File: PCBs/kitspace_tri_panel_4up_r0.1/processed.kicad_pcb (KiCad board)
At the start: 4 copper layers, 105.3 x 45.2 mm, 660 parts, among them J1 input, J2 output, Q1 LP0404N3T5G, Q10 LP0404N3T5G, Q11 LP0404N3T5G, Q12 LP0404N3T5G, Q13 LP0404N3T5G, Q14 LP0404N3T5G, Q15 LP0404N3T5G, Q2 LP0404N3T5G, Q3 LP0404N3T5G, Q4 LP0404N3T5G, Q5 LP0404N3T5G, Q6 LP0404N3T5G, Q7 LP0404N3T5G, Q8 LP0404N3T5G, Q9 LP0404N3T5G, U1 TLC59025, U2 TLC59025, U3 TLC59025, U4 74HC595, U5 74HC595

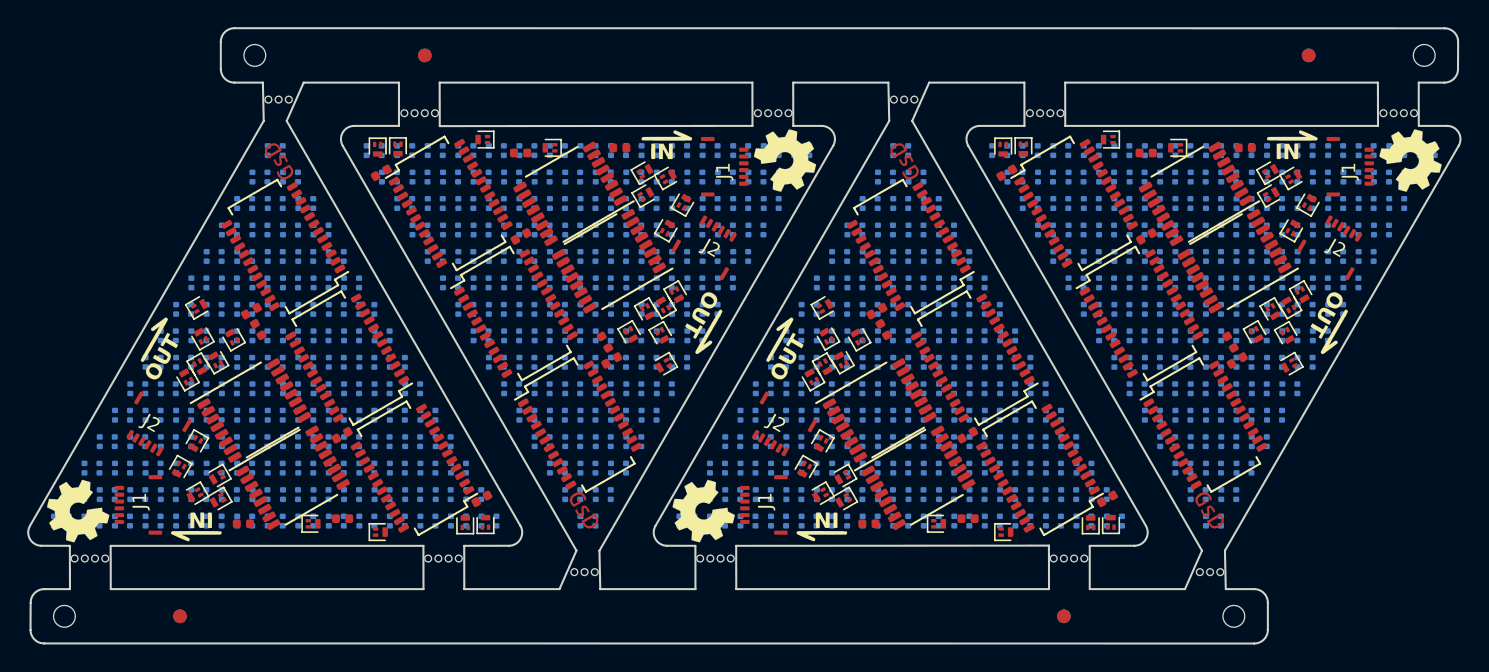
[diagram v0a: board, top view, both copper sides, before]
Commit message: recheck all circuits and clean up fill zone by rerouting the nets using freerouting and manually
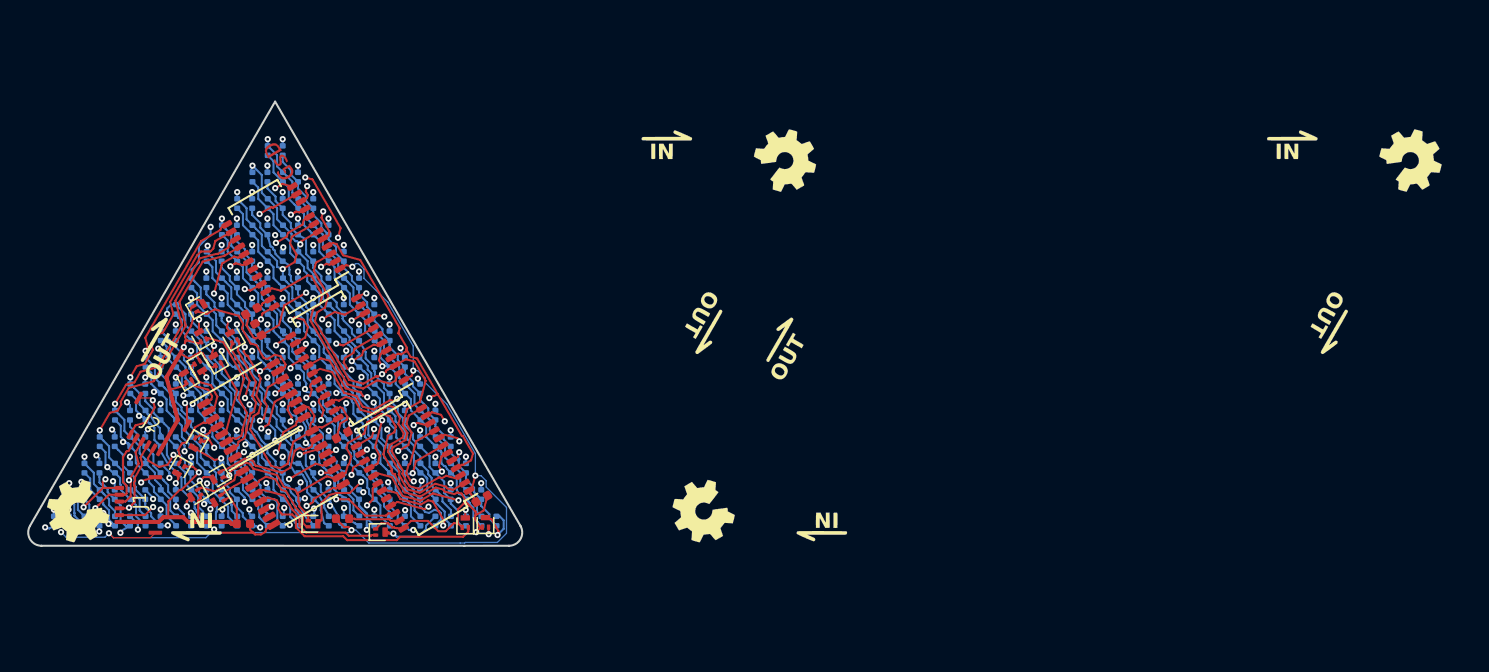
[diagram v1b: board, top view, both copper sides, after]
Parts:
- removed ? (x4): , MountingHole:MountingHole_2.1mm
- removed the C1 at (121.8, 91.6)
- removed the C1 at (167.8, 91.6)
- removed the C1 at (175.2, 115.6)
- removed the C2 at (138.2, 104.1)
- removed the C2 at (184.2, 104.1)
- removed the C2 at (158.8, 103.2)
- removed the C3 at (139.3, 89.8)
- removed the C3 at (185.3, 89.8)
- removed the C3 at (157.7, 117.4)
- removed the D1 at (137.0, 117.2)
- removed the D1 at (183.0, 117.2)
- removed the D1 at (160.0, 90.0)
- removed the D10 at (147.1, 99.7)
- removed the D10 at (193.1, 99.7)
- removed the D10 at (149.9, 107.5)
- removed the D100 at (133.6, 99.7)
- removed the D100 at (179.6, 99.7)
- removed the D100 at (163.4, 107.5)
- removed the D101 at (134.8, 97.8)
- removed the D101 at (180.8, 97.8)
- removed the D101 at (162.2, 109.5)
- removed the D102 at (135.9, 95.8)
- removed the D102 at (181.9, 95.8)
- removed the D102 at (161.1, 111.4)
- removed the D103 at (137.0, 93.9)
- removed the D103 at (183.0, 93.9)
- removed the D103 at (160.0, 113.4)
- removed the D104 at (138.1, 91.9)
- removed the D104 at (184.1, 91.9)
- removed the D104 at (158.9, 115.3)
- removed the D105 at (139.2, 90.0)
- removed the D105 at (185.2, 90.0)
- removed the D105 at (157.8, 117.2)
- removed the D11 at (148.2, 97.8)
- removed the D11 at (194.2, 97.8)
- removed the D11 at (148.8, 109.5)
- removed the D113 at (129.1, 103.6)
- removed the D113 at (175.1, 103.6)
- removed the D113 at (167.9, 103.6)
- removed the D114 at (130.3, 101.7)
- removed the D114 at (176.3, 101.7)
- removed the D114 at (166.7, 105.6)
- removed the D115 at (131.4, 99.7)
- removed the D115 at (177.4, 99.7)
- removed the D115 at (165.6, 107.5)
- removed the D116 at (132.5, 97.8)
- removed the D116 at (178.5, 97.8)
- removed the D116 at (164.5, 109.5)
- removed the D117 at (133.6, 95.8)
- removed the D117 at (179.6, 95.8)
- removed the D117 at (163.4, 111.4)
- removed the D118 at (134.8, 93.9)
- removed the D118 at (180.8, 93.9)
- removed the D118 at (162.2, 113.4)
- removed the D119 at (135.9, 91.9)
- removed the D119 at (181.9, 91.9)
- removed the D119 at (161.1, 115.3)
- removed the D12 at (149.4, 95.8)
- removed the D12 at (195.4, 95.8)
- removed the D12 at (147.6, 111.4)
- removed the D120 at (137.0, 90.0)
- removed the D120 at (183.0, 90.0)
- removed the D120 at (160.0, 117.2)
- removed the D129 at (128.0, 101.7)
- removed the D129 at (174.0, 101.7)
- removed the D129 at (169.0, 105.6)
- removed the D13 at (150.5, 93.9)
- removed the D13 at (196.5, 93.9)
- removed the D13 at (146.5, 113.4)
- removed the D130 at (129.1, 99.7)
- removed the D130 at (175.1, 99.7)
- removed the D130 at (167.9, 107.5)
- removed the D131 at (130.3, 97.8)
- removed the D131 at (176.3, 97.8)
- removed the D131 at (166.7, 109.5)
- removed the D132 at (131.4, 95.8)
- removed the D132 at (177.4, 95.8)
- removed the D132 at (165.6, 111.4)
- removed the D133 at (132.5, 93.9)
- removed the D133 at (178.5, 93.9)
- removed the D133 at (164.5, 113.4)
- removed the D134 at (133.6, 91.9)
- removed the D134 at (179.6, 91.9)
- removed the D134 at (163.4, 115.3)
- removed the D135 at (134.8, 90.0)
- removed the D135 at (180.8, 90.0)
- removed the D135 at (162.2, 117.2)
- removed the D14 at (151.6, 91.9)
- removed the D14 at (197.6, 91.9)
- removed the D14 at (145.4, 115.3)
- removed the D145 at (126.9, 99.7)
- removed the D145 at (172.9, 99.7)
- removed the D145 at (170.1, 107.5)
- removed the D146 at (128.0, 97.8)
- removed the D146 at (174.0, 97.8)
- removed the D146 at (169.0, 109.5)
- removed the D147 at (129.1, 95.8)
- removed the D147 at (175.1, 95.8)
- removed the D147 at (167.9, 111.4)
- removed the D148 at (130.3, 93.9)
- removed the D148 at (176.3, 93.9)
- removed the D148 at (166.7, 113.4)
- removed the D149 at (131.4, 91.9)
- removed the D149 at (177.4, 91.9)
- removed the D149 at (165.6, 115.3)
- removed the D15 at (152.7, 90.0)
- removed the D15 at (198.7, 90.0)
- removed the D15 at (144.3, 117.2)
- removed the D150 at (132.5, 90.0)
- removed the D150 at (178.5, 90.0)
- removed the D150 at (164.5, 117.2)
- removed the D161 at (125.8, 97.8)
- removed the D161 at (171.8, 97.8)
- removed the D161 at (171.2, 109.5)
- removed the D162 at (126.9, 95.8)
- removed the D162 at (172.9, 95.8)
- removed the D162 at (170.1, 111.4)
- removed the D163 at (128.0, 93.9)
- removed the D163 at (174.0, 93.9)
- removed the D163 at (169.0, 113.4)
- removed the D164 at (129.1, 91.9)
- removed the D164 at (175.1, 91.9)
- removed the D164 at (167.9, 115.3)
- removed the D165 at (130.3, 90.0)
- removed the D165 at (176.3, 90.0)
- removed the D165 at (166.7, 117.2)
- removed the D17 at (135.9, 115.3)
- removed the D17 at (181.9, 115.3)
- removed the D17 at (161.1, 91.9)
- removed the D177 at (124.6, 95.8)
- removed the D177 at (170.6, 95.8)
- removed the D177 at (172.4, 111.4)
- removed the D178 at (125.8, 93.9)
- removed the D178 at (171.8, 93.9)
- removed the D178 at (171.2, 113.4)
- removed the D179 at (126.9, 91.9)
- removed the D179 at (172.9, 91.9)
- removed the D179 at (170.1, 115.3)
- removed the D18 at (137.0, 113.4)
- removed the D18 at (183.0, 113.4)
- removed the D18 at (160.0, 93.9)
- removed the D180 at (128.0, 90.0)
- removed the D180 at (174.0, 90.0)
- removed the D180 at (169.0, 117.2)
- removed the D19 at (138.1, 111.4)
- removed the D19 at (184.1, 111.4)
- removed the D19 at (158.9, 95.8)
- removed the D193 at (123.5, 93.9)
- removed the D193 at (169.5, 93.9)
- removed the D193 at (173.5, 113.4)
- removed the D194 at (124.6, 91.9)
- removed the D194 at (170.6, 91.9)
- removed the D194 at (172.4, 115.3)
- removed the D195 at (125.8, 90.0)
- removed the D195 at (171.8, 90.0)
- removed the D195 at (171.2, 117.2)
- removed the D2 at (138.1, 115.3)
- removed the D2 at (184.1, 115.3)
- removed the D2 at (158.9, 91.9)
- removed the D20 at (139.2, 109.5)
- removed the D20 at (185.2, 109.5)
- removed the D20 at (157.8, 97.8)
- removed the D209 at (122.4, 91.9)
- removed the D209 at (168.4, 91.9)
- removed the D209 at (174.6, 115.3)
- removed the D21 at (140.4, 107.5)
- removed the D21 at (186.4, 107.5)
- removed the D21 at (156.6, 99.7)
- removed the D210 at (123.5, 90.0)
- removed the D210 at (169.5, 90.0)
- removed the D210 at (173.5, 117.2)
- removed the D22 at (141.5, 105.6)
- removed the D22 at (187.5, 105.6)
- removed the D22 at (155.5, 101.7)
- removed the D225 at (121.3, 90.0)
- removed the D225 at (167.3, 90.0)
- removed the D225 at (175.7, 117.2)
- removed the D23 at (142.6, 103.6)
- removed the D23 at (188.6, 103.6)
- removed the D23 at (154.4, 103.6)
- removed the D24 at (143.7, 101.7)
- removed the D24 at (189.7, 101.7)
- removed the D24 at (153.3, 105.6)
- removed the D25 at (144.9, 99.7)
- removed the D25 at (190.9, 99.7)
- removed the D25 at (152.1, 107.5)
- removed the D26 at (146.0, 97.8)
- removed the D26 at (192.0, 97.8)
- removed the D26 at (151.0, 109.5)
- removed the D27 at (147.1, 95.8)
- removed the D27 at (193.1, 95.8)
- removed the D27 at (149.9, 111.4)
- removed the D28 at (148.2, 93.9)
- removed the D28 at (194.2, 93.9)
- removed the D28 at (148.8, 113.4)
- removed the D29 at (149.4, 91.9)
- removed the D29 at (195.4, 91.9)
- removed the D29 at (147.6, 115.3)
- removed the D3 at (139.2, 113.4)
- removed the D3 at (185.2, 113.4)
- removed the D3 at (157.8, 93.9)
- removed the D30 at (150.5, 90.0)
- removed the D30 at (196.5, 90.0)
- removed the D30 at (146.5, 117.2)
- removed the D33 at (134.8, 113.4)
- removed the D33 at (180.8, 113.4)
- removed the D33 at (162.2, 93.9)
- removed the D34 at (135.9, 111.4)
- removed the D34 at (181.9, 111.4)
- removed the D34 at (161.1, 95.8)
- removed the D35 at (137.0, 109.5)
- removed the D35 at (183.0, 109.5)
- removed the D35 at (160.0, 97.8)
- removed the D36 at (138.1, 107.5)
- removed the D36 at (184.1, 107.5)
- removed the D36 at (158.9, 99.7)
- removed the D37 at (139.2, 105.6)
- removed the D37 at (185.2, 105.6)
- removed the D37 at (157.8, 101.7)
- removed the D38 at (140.4, 103.6)
- removed the D38 at (186.4, 103.6)
- removed the D38 at (156.6, 103.6)
- removed the D39 at (141.5, 101.7)
- removed the D39 at (187.5, 101.7)
- removed the D39 at (155.5, 105.6)
- removed the D4 at (140.4, 111.4)
- removed the D4 at (186.4, 111.4)
- removed the D4 at (156.6, 95.8)
- removed the D40 at (142.6, 99.7)
- removed the D40 at (188.6, 99.7)
- removed the D40 at (154.4, 107.5)
- removed the D41 at (143.7, 97.8)
- removed the D41 at (189.7, 97.8)
- removed the D41 at (153.3, 109.5)
- removed the D42 at (144.9, 95.8)
- removed the D42 at (190.9, 95.8)
- removed the D42 at (152.1, 111.4)
- removed the D43 at (146.0, 93.9)
- removed the D43 at (192.0, 93.9)
- removed the D43 at (151.0, 113.4)
- removed the D44 at (147.1, 91.9)
- removed the D44 at (193.1, 91.9)
- removed the D44 at (149.9, 115.3)
- removed the D45 at (148.2, 90.0)
- removed the D45 at (194.2, 90.0)
- removed the D45 at (148.8, 117.2)
- removed the D49 at (133.6, 111.4)
- removed the D49 at (179.6, 111.4)
- removed the D49 at (163.4, 95.8)
- removed the D5 at (141.5, 109.5)
- removed the D5 at (187.5, 109.5)
- removed the D5 at (155.5, 97.8)
- removed the D50 at (134.8, 109.5)
- removed the D50 at (180.8, 109.5)
- removed the D50 at (162.2, 97.8)
- removed the D51 at (135.9, 107.5)
- removed the D51 at (181.9, 107.5)
- removed the D51 at (161.1, 99.7)
- removed the D52 at (137.0, 105.6)
- removed the D52 at (183.0, 105.6)
- removed the D52 at (160.0, 101.7)
- removed the D53 at (138.1, 103.6)
- removed the D53 at (184.1, 103.6)
- removed the D53 at (158.9, 103.6)
- removed the D54 at (139.2, 101.7)
- removed the D54 at (185.2, 101.7)
- removed the D54 at (157.8, 105.6)
- removed the D55 at (140.4, 99.7)
- removed the D55 at (186.4, 99.7)
- removed the D55 at (156.6, 107.5)
- removed the D56 at (141.5, 97.8)
- removed the D56 at (187.5, 97.8)
- removed the D56 at (155.5, 109.5)
- removed the D57 at (142.6, 95.8)
- removed the D57 at (188.6, 95.8)
- removed the D57 at (154.4, 111.4)
- removed the D58 at (143.7, 93.9)
- removed the D58 at (189.7, 93.9)
- removed the D58 at (153.3, 113.4)
- removed the D59 at (144.9, 91.9)
- removed the D59 at (190.9, 91.9)
- removed the D59 at (152.1, 115.3)
- removed the D6 at (142.6, 107.5)
- removed the D6 at (188.6, 107.5)
- removed the D6 at (154.4, 99.7)
- removed the D60 at (146.0, 90.0)
- removed the D60 at (192.0, 90.0)
- removed the D60 at (151.0, 117.2)
- removed the D65 at (132.5, 109.5)
- removed the D65 at (178.5, 109.5)
- removed the D65 at (164.5, 97.8)
- removed the D66 at (133.6, 107.5)
- removed the D66 at (179.6, 107.5)
- removed the D66 at (163.4, 99.7)
- removed the D67 at (134.8, 105.6)
- removed the D67 at (180.8, 105.6)
- removed the D67 at (162.2, 101.7)
- removed the D68 at (135.9, 103.6)
- removed the D68 at (181.9, 103.6)
- removed the D68 at (161.1, 103.6)
- removed the D69 at (137.0, 101.7)
- removed the D69 at (183.0, 101.7)
- removed the D69 at (160.0, 105.6)
- removed the D7 at (143.7, 105.6)
- removed the D7 at (189.7, 105.6)
- removed the D7 at (153.3, 101.7)
- removed the D70 at (138.1, 99.7)
- removed the D70 at (184.1, 99.7)
- removed the D70 at (158.9, 107.5)
- removed the D71 at (139.2, 97.8)
- removed the D71 at (185.2, 97.8)
- removed the D71 at (157.8, 109.5)
- removed the D72 at (140.4, 95.8)
- removed the D72 at (186.4, 95.8)
- removed the D72 at (156.6, 111.4)
- removed the D73 at (141.5, 93.9)
- removed the D73 at (187.5, 93.9)
- removed the D73 at (155.5, 113.4)
- removed the D74 at (142.6, 91.9)
- removed the D74 at (188.6, 91.9)
- removed the D74 at (154.4, 115.3)
- removed the D75 at (143.7, 90.0)
- removed the D75 at (189.7, 90.0)
- removed the D75 at (153.3, 117.2)
- removed the D8 at (144.9, 103.6)
- removed the D8 at (190.9, 103.6)
- removed the D8 at (152.1, 103.6)
- removed the D81 at (131.4, 107.5)
- removed the D81 at (177.4, 107.5)
- removed the D81 at (165.6, 99.7)
- removed the D82 at (132.5, 105.6)
- removed the D82 at (178.5, 105.6)
- removed the D82 at (164.5, 101.7)
- removed the D83 at (133.6, 103.6)
- removed the D83 at (179.6, 103.6)
- removed the D83 at (163.4, 103.6)
- removed the D84 at (134.8, 101.7)
- removed the D84 at (180.8, 101.7)
- removed the D84 at (162.2, 105.6)
- removed the D85 at (135.9, 99.7)
- removed the D85 at (181.9, 99.7)
- removed the D85 at (161.1, 107.5)
- removed the D86 at (137.0, 97.8)
- removed the D86 at (183.0, 97.8)
- removed the D86 at (160.0, 109.5)
- removed the D87 at (138.1, 95.8)
- removed the D87 at (184.1, 95.8)
- removed the D87 at (158.9, 111.4)
- removed the D88 at (139.2, 93.9)
- removed the D88 at (185.2, 93.9)
- removed the D88 at (157.8, 113.4)
- removed the D89 at (140.4, 91.9)
- removed the D89 at (186.4, 91.9)
- removed the D89 at (156.6, 115.3)
- removed the D9 at (146.0, 101.7)
- removed the D9 at (192.0, 101.7)
- removed the D9 at (151.0, 105.6)
- removed the D90 at (141.5, 90.0)
- removed the D90 at (187.5, 90.0)
- removed the D90 at (155.5, 117.2)
- removed the D97 at (130.3, 105.6)
- removed the D97 at (176.3, 105.6)
- removed the D97 at (166.7, 101.7)
- removed the D98 at (131.4, 103.6)
- removed the D98 at (177.4, 103.6)
- removed the D98 at (165.6, 103.6)
- removed the D99 at (132.5, 101.7)
- removed the D99 at (178.5, 101.7)
- removed the D99 at (164.5, 105.6)
- removed the G*** at (136.6, 116.5)
- removed the G*** at (182.6, 116.5)
- removed the G*** at (160.4, 90.7)
- removed the J1 at (148.5, 91.2)
- removed the J1 at (194.5, 91.2)
- removed the J1 at (148.5, 116.1)
- removed the J2 at (146.6, 95.7)
- removed the J2 at (192.6, 95.7)
- removed the J2 at (150.4, 111.5)
- removed the Q1 at (142.6, 105.8)
- removed the Q1 at (188.6, 105.8)
- removed the Q1 at (154.4, 101.5)
- removed the Q10 at (142.9, 91.9)
- removed the Q10 at (188.9, 91.9)
- removed the Q10 at (154.1, 115.3)
- removed the Q11 at (141.2, 91.5)
- removed the Q11 at (187.2, 91.5)
- removed the Q11 at (155.8, 115.7)
- removed the Q12 at (134.2, 89.8)
- removed the Q12 at (180.2, 89.8)
- removed the Q12 at (162.8, 117.4)
- removed the Q13 at (129.3, 89.2)
- removed the Q13 at (175.3, 89.2)
- removed the Q13 at (167.7, 118.1)
- removed the Q14 at (123.0, 89.9)
- removed the Q14 at (169.0, 89.9)
- removed the Q14 at (174.0, 117.4)
- removed the Q15 at (121.5, 89.9)
- removed the Q15 at (167.5, 89.9)
- removed the Q15 at (175.5, 117.3)
- removed the Q2 at (143.5, 100.6)
- removed the Q2 at (189.5, 100.6)
- removed the Q2 at (153.5, 106.7)
- removed the Q3 at (142.6, 101.4)
- removed the Q3 at (188.6, 101.4)
- removed the Q3 at (154.4, 105.9)
- removed the Q4 at (144.1, 93.8)
- removed the Q4 at (190.1, 93.8)
- removed the Q4 at (152.9, 113.4)
- removed the Q5 at (142.8, 95.7)
- removed the Q5 at (188.8, 95.7)
- removed the Q5 at (154.2, 111.5)
- removed the Q6 at (141.4, 101.8)
- removed the Q6 at (187.4, 101.8)
- removed the Q6 at (155.6, 105.4)
- removed the Q7 at (142.4, 103.6)
- removed the Q7 at (188.4, 103.6)
- removed the Q7 at (154.6, 103.7)
- removed the Q8 at (140.1, 103.5)
- removed the Q8 at (186.1, 103.5)
- removed the Q8 at (156.9, 103.7)
- removed the Q9 at (141.3, 93.2)
- removed the Q9 at (187.3, 93.2)
- removed the Q9 at (155.7, 114.0)
- removed the R1 at (138.8, 105.4)
- removed the R1 at (184.8, 105.4)
- removed the R1 at (158.2, 101.8)
- removed the R2 at (132.1, 96.3)
- removed the R2 at (178.1, 96.3)
- removed the R2 at (164.9, 110.9)
- removed the R3 at (132.0, 90.2)
- removed the R3 at (178.0, 90.2)
- removed the R3 at (165.0, 117.1)
- removed the REF** at (107.0, 124.2) (x2)
- removed the REF** at (100.8, 120.0)
- removed the REF** at (99.2, 120.0)
- removed the REF** at (125.2, 120.0)
- removed the REF** at (100.0, 120.0)
- removed the REF** at (136.8, 121.0)
- removed the REF** at (126.8, 120.0)
- removed the REF** at (127.5, 120.0)
- removed the REF** at (136.0, 121.0)
- removed the REF** at (183.5, 121.0)
- removed the REF** at (182.8, 121.0)
- removed the REF** at (172.0, 124.2) (x2)
- removed the REF** at (182.0, 121.0)
- removed the REF** at (173.5, 120.0)
- removed the REF** at (172.8, 120.0)
- removed the REF** at (172.0, 120.0)
- removed the REF** at (171.2, 120.0)
- removed the REF** at (147.5, 120.0)
- removed the REF** at (146.8, 120.0)
- removed the REF** at (146.0, 120.0)
- removed the REF** at (145.2, 120.0)
- removed the REF** at (159.5, 86.2)
- removed the REF** at (160.2, 86.2)
- removed the REF** at (161.0, 86.2)
- removed the REF** at (169.5, 87.2)
- removed the REF** at (170.2, 87.2)
- removed the REF** at (171.0, 87.2)
- removed the REF** at (171.8, 87.2)
- removed the REF** at (195.5, 87.2)
- removed the REF** at (196.2, 87.2)
- removed the REF** at (197.0, 87.2)
- removed the REF** at (197.8, 87.2)
- removed the REF** at (151.8, 87.2)
- removed the REF** at (151.0, 87.2)
- removed the REF** at (150.2, 87.2)
- removed the REF** at (149.5, 87.2)
- removed the REF** at (125.8, 87.2)
- removed the REF** at (125.0, 87.2)
- removed the REF** at (124.2, 87.2)
- removed the REF** at (190.0, 83.0) (x2)
- removed the REF** at (123.5, 87.2)
- removed the REF** at (115.0, 86.2)
- removed the REF** at (114.2, 86.2)
- removed the REF** at (113.5, 86.2)
- removed the REF** at (125.0, 83.0) (x2)
- removed the REF** at (126.0, 120.0)
- removed the REF** at (101.5, 120.0)
- removed the REF** at (137.5, 121.0)
- removed the U1 at (136.4, 110.2)
- removed the U1 at (182.4, 110.2)
- removed the U1 at (160.6, 97.1)
- removed the U2 at (131.7, 102.0)
- removed the U2 at (177.7, 102.0)
- removed the U2 at (165.3, 105.3)
- removed the U3 at (126.9, 93.9)
- removed the U3 at (172.9, 93.9)
- removed the U3 at (170.1, 113.4)
- removed the U4 at (138.6, 98.1)
- removed the U4 at (184.6, 98.1)
- removed the U4 at (158.4, 109.1)
- removed the U5 at (135.7, 93.2)
- removed the U5 at (181.7, 93.2)
- removed the U5 at (161.3, 114.1)
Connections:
- C1 pad 1: (no net) -> vcc
- C1 pad 2: (no net) -> gnd
- C2 pad 1: (no net) -> vcc
- C2 pad 2: (no net) -> gnd
- C3 pad 1: (no net) -> vcc
- C3 pad 2: (no net) -> gnd
- D1 pad 1: (no net) -> row_0
- D1 pad 2: (no net) -> colr_0
- D1 pad 3: (no net) -> colg_0
- D1 pad 4: (no net) -> colb_0
- D10 pad 1: (no net) -> row_0
- D10 pad 2: (no net) -> colr_9
- D10 pad 3: (no net) -> colg_9
- D10 pad 4: (no net) -> colb_9
- D100 pad 1: (no net) -> row_6
- D100 pad 2: (no net) -> colr_3
- D100 pad 3: (no net) -> colg_3
- D100 pad 4: (no net) -> colb_3
- D101 pad 1: (no net) -> row_6
- D101 pad 2: (no net) -> colr_4
- D101 pad 3: (no net) -> colg_4
- D101 pad 4: (no net) -> colb_4
- D102 pad 1: (no net) -> row_6
- D102 pad 2: (no net) -> colr_5
- D102 pad 3: (no net) -> colg_5
- D102 pad 4: (no net) -> colb_5
- D103 pad 1: (no net) -> row_6
- D103 pad 2: (no net) -> colr_6
- D103 pad 3: (no net) -> colg_6
- D103 pad 4: (no net) -> colb_6
- D104 pad 1: (no net) -> row_6
- D104 pad 2: (no net) -> colr_7
- D104 pad 3: (no net) -> colg_7
- D104 pad 4: (no net) -> colb_7
- D105 pad 1: (no net) -> row_6
- D105 pad 2: (no net) -> colr_8
- D105 pad 3: (no net) -> colg_8
- D105 pad 4: (no net) -> colb_8
- D11 pad 1: (no net) -> row_0
- D11 pad 2: (no net) -> colr_10
- D11 pad 3: (no net) -> colg_10
- D11 pad 4: (no net) -> colb_10
- D113 pad 1: (no net) -> row_7
- D113 pad 2: (no net) -> colr_0
- D113 pad 3: (no net) -> colg_0
- D113 pad 4: (no net) -> colb_0
- D114 pad 1: (no net) -> row_7
- D114 pad 2: (no net) -> colr_1
- D114 pad 3: (no net) -> colg_1
- D114 pad 4: (no net) -> colb_1
- D115 pad 1: (no net) -> row_7
- D115 pad 2: (no net) -> colr_2
- D115 pad 3: (no net) -> colg_2
- D115 pad 4: (no net) -> colb_2
- D116 pad 1: (no net) -> row_7
- D116 pad 2: (no net) -> colr_3
- D116 pad 3: (no net) -> colg_3
- D116 pad 4: (no net) -> colb_3
- D117 pad 1: (no net) -> row_7
- D117 pad 2: (no net) -> colr_4
- D117 pad 3: (no net) -> colg_4
- D117 pad 4: (no net) -> colb_4
- D118 pad 1: (no net) -> row_7
- D118 pad 2: (no net) -> colr_5
- D118 pad 3: (no net) -> colg_5
- D118 pad 4: (no net) -> colb_5
- D119 pad 1: (no net) -> row_7
- D119 pad 2: (no net) -> colr_6
- D119 pad 3: (no net) -> colg_6
- D119 pad 4: (no net) -> colb_6
- D12 pad 1: (no net) -> row_0
- D12 pad 2: (no net) -> colr_11
- D12 pad 3: (no net) -> colg_11
- D12 pad 4: (no net) -> colb_11
- D120 pad 1: (no net) -> row_7
- D120 pad 2: (no net) -> colr_7
- D120 pad 3: (no net) -> colg_7
- D120 pad 4: (no net) -> colb_7
- D129 pad 1: (no net) -> row_8
- D129 pad 2: (no net) -> colr_0
- D129 pad 3: (no net) -> colg_0
- D129 pad 4: (no net) -> colb_0
- D13 pad 1: (no net) -> row_0
- D13 pad 2: (no net) -> colr_12
- D13 pad 3: (no net) -> colg_12
- D13 pad 4: (no net) -> colb_12
- D130 pad 1: (no net) -> row_8
- D130 pad 2: (no net) -> colr_1
- D130 pad 3: (no net) -> colg_1
- D130 pad 4: (no net) -> colb_1
- D131 pad 1: (no net) -> row_8
- D131 pad 2: (no net) -> colr_2
- D131 pad 3: (no net) -> colg_2
- D131 pad 4: (no net) -> colb_2
- D132 pad 1: (no net) -> row_8
- D132 pad 2: (no net) -> colr_3
- D132 pad 3: (no net) -> colg_3
- D132 pad 4: (no net) -> colb_3
- D133 pad 1: (no net) -> row_8
- D133 pad 2: (no net) -> colr_4
- D133 pad 3: (no net) -> colg_4
- D133 pad 4: (no net) -> colb_4
- D134 pad 1: (no net) -> row_8
- D134 pad 2: (no net) -> colr_5
- D134 pad 3: (no net) -> colg_5
- D134 pad 4: (no net) -> colb_5
- D135 pad 1: (no net) -> row_8
- D135 pad 2: (no net) -> colr_6
- D135 pad 3: (no net) -> colg_6
- D135 pad 4: (no net) -> colb_6
- D14 pad 1: (no net) -> row_0
- D14 pad 2: (no net) -> colr_13
- D14 pad 3: (no net) -> colg_13
- D14 pad 4: (no net) -> colb_13
- D145 pad 1: (no net) -> row_9
- D145 pad 2: (no net) -> colr_0
- D145 pad 3: (no net) -> colg_0
- D145 pad 4: (no net) -> colb_0
- D146 pad 1: (no net) -> row_9
- D146 pad 2: (no net) -> colr_1
- D146 pad 3: (no net) -> colg_1
- D146 pad 4: (no net) -> colb_1
- D147 pad 1: (no net) -> row_9
- D147 pad 2: (no net) -> colr_2
- D147 pad 3: (no net) -> colg_2
- D147 pad 4: (no net) -> colb_2
- D148 pad 1: (no net) -> row_9
- D148 pad 2: (no net) -> colr_3
- D148 pad 3: (no net) -> colg_3
- D148 pad 4: (no net) -> colb_3
- D149 pad 1: (no net) -> row_9
- D149 pad 2: (no net) -> colr_4
- D149 pad 3: (no net) -> colg_4
- D149 pad 4: (no net) -> colb_4
- D15 pad 1: (no net) -> row_0
- D15 pad 2: (no net) -> colr_14
- D15 pad 3: (no net) -> colg_14
- D15 pad 4: (no net) -> colb_14
- D150 pad 1: (no net) -> row_9
- D150 pad 2: (no net) -> colr_5
- D150 pad 3: (no net) -> colg_5
- D150 pad 4: (no net) -> colb_5
- D161 pad 1: (no net) -> row_10
- D161 pad 2: (no net) -> colr_0
- D161 pad 3: (no net) -> colg_0
- D161 pad 4: (no net) -> colb_0
- D162 pad 1: (no net) -> row_10
- D162 pad 2: (no net) -> colr_1
- D162 pad 3: (no net) -> colg_1
- D162 pad 4: (no net) -> colb_1
- D163 pad 1: (no net) -> row_10
- D163 pad 2: (no net) -> colr_2
- D163 pad 3: (no net) -> colg_2
- D163 pad 4: (no net) -> colb_2
- D164 pad 1: (no net) -> row_10
- D164 pad 2: (no net) -> colr_3
- D164 pad 3: (no net) -> colg_3
- D164 pad 4: (no net) -> colb_3
- D165 pad 1: (no net) -> row_10
- D165 pad 2: (no net) -> colr_4
- D165 pad 3: (no net) -> colg_4
- D165 pad 4: (no net) -> colb_4
- D17 pad 1: (no net) -> row_1
- D17 pad 2: (no net) -> colr_0
- D17 pad 3: (no net) -> colg_0
- D17 pad 4: (no net) -> colb_0
- D177 pad 1: (no net) -> row_11
- D177 pad 2: (no net) -> colr_0
- D177 pad 3: (no net) -> colg_0
- D177 pad 4: (no net) -> colb_0
- D178 pad 1: (no net) -> row_11
- D178 pad 2: (no net) -> colr_1
- D178 pad 3: (no net) -> colg_1
- D178 pad 4: (no net) -> colb_1
- D179 pad 1: (no net) -> row_11
- D179 pad 2: (no net) -> colr_2
- D179 pad 3: (no net) -> colg_2
- D179 pad 4: (no net) -> colb_2
- D18 pad 1: (no net) -> row_1
- D18 pad 2: (no net) -> colr_1
- D18 pad 3: (no net) -> colg_1
- D18 pad 4: (no net) -> colb_1
- D180 pad 1: (no net) -> row_11
- D180 pad 2: (no net) -> colr_3
- D180 pad 3: (no net) -> colg_3
- D180 pad 4: (no net) -> colb_3
- D19 pad 1: (no net) -> row_1
- D19 pad 2: (no net) -> colr_2
- D19 pad 3: (no net) -> colg_2
- D19 pad 4: (no net) -> colb_2
- D193 pad 1: (no net) -> row_12
- D193 pad 2: (no net) -> colr_0
- D193 pad 3: (no net) -> colg_0
- D193 pad 4: (no net) -> colb_0
- D194 pad 1: (no net) -> row_12
- D194 pad 2: (no net) -> colr_1
- D194 pad 3: (no net) -> colg_1
- D194 pad 4: (no net) -> colb_1
- D195 pad 1: (no net) -> row_12
- D195 pad 2: (no net) -> colr_2
- D195 pad 3: (no net) -> colg_2
- D195 pad 4: (no net) -> colb_2
- D2 pad 1: (no net) -> row_0
- D2 pad 2: (no net) -> colr_1
- D2 pad 3: (no net) -> colg_1
- D2 pad 4: (no net) -> colb_1
- D20 pad 1: (no net) -> row_1
- D20 pad 2: (no net) -> colr_3
- D20 pad 3: (no net) -> colg_3
- D20 pad 4: (no net) -> colb_3
- D209 pad 1: (no net) -> row_13
- D209 pad 2: (no net) -> colr_0
- D209 pad 3: (no net) -> colg_0
- D209 pad 4: (no net) -> colb_0
- D21 pad 1: (no net) -> row_1
- D21 pad 2: (no net) -> colr_4
- D21 pad 3: (no net) -> colg_4
- D21 pad 4: (no net) -> colb_4
- D210 pad 1: (no net) -> row_13
- D210 pad 2: (no net) -> colr_1
- D210 pad 3: (no net) -> colg_1
- D210 pad 4: (no net) -> colb_1
- D22 pad 1: (no net) -> row_1
- D22 pad 2: (no net) -> colr_5
- D22 pad 3: (no net) -> colg_5
- D22 pad 4: (no net) -> colb_5
- D225 pad 1: (no net) -> row_14
- D225 pad 2: (no net) -> colr_0
- D225 pad 3: (no net) -> colg_0
- D225 pad 4: (no net) -> colb_0
- D23 pad 1: (no net) -> row_1
- D23 pad 2: (no net) -> colr_6
- D23 pad 3: (no net) -> colg_6
- D23 pad 4: (no net) -> colb_6
- D24 pad 1: (no net) -> row_1
- D24 pad 2: (no net) -> colr_7
- D24 pad 3: (no net) -> colg_7
- D24 pad 4: (no net) -> colb_7
- D25 pad 1: (no net) -> row_1
- D25 pad 2: (no net) -> colr_8
- D25 pad 3: (no net) -> colg_8
- D25 pad 4: (no net) -> colb_8
- D26 pad 1: (no net) -> row_1
- D26 pad 2: (no net) -> colr_9
- D26 pad 3: (no net) -> colg_9
- D26 pad 4: (no net) -> colb_9
- D27 pad 1: (no net) -> row_1
- D27 pad 2: (no net) -> colr_10
- D27 pad 3: (no net) -> colg_10
- D27 pad 4: (no net) -> colb_10
- D28 pad 1: (no net) -> row_1
- D28 pad 2: (no net) -> colr_11
- D28 pad 3: (no net) -> colg_11
- D28 pad 4: (no net) -> colb_11
- D29 pad 1: (no net) -> row_1
- D29 pad 2: (no net) -> colr_12
- D29 pad 3: (no net) -> colg_12
- D29 pad 4: (no net) -> colb_12
- D3 pad 1: (no net) -> row_0
- D3 pad 2: (no net) -> colr_2
- D3 pad 3: (no net) -> colg_2
- D3 pad 4: (no net) -> colb_2
- D30 pad 1: (no net) -> row_1
- D30 pad 2: (no net) -> colr_13
- D30 pad 3: (no net) -> colg_13
- D30 pad 4: (no net) -> colb_13
- D33 pad 1: (no net) -> row_2
- D33 pad 2: (no net) -> colr_0
- D33 pad 3: (no net) -> colg_0
- D33 pad 4: (no net) -> colb_0
- D34 pad 1: (no net) -> row_2
- D34 pad 2: (no net) -> colr_1
- D34 pad 3: (no net) -> colg_1
- D34 pad 4: (no net) -> colb_1
- D35 pad 1: (no net) -> row_2
- D35 pad 2: (no net) -> colr_2
- D35 pad 3: (no net) -> colg_2
- D35 pad 4: (no net) -> colb_2
- D36 pad 1: (no net) -> row_2
- D36 pad 2: (no net) -> colr_3
- D36 pad 3: (no net) -> colg_3
- D36 pad 4: (no net) -> colb_3
- D37 pad 1: (no net) -> row_2
- D37 pad 2: (no net) -> colr_4
- D37 pad 3: (no net) -> colg_4
- D37 pad 4: (no net) -> colb_4
- D38 pad 1: (no net) -> row_2
- D38 pad 2: (no net) -> colr_5
- D38 pad 3: (no net) -> colg_5
- D38 pad 4: (no net) -> colb_5
- D39 pad 1: (no net) -> row_2
- D39 pad 2: (no net) -> colr_6
- D39 pad 3: (no net) -> colg_6
- D39 pad 4: (no net) -> colb_6
- D4 pad 1: (no net) -> row_0
- D4 pad 2: (no net) -> colr_3
- D4 pad 3: (no net) -> colg_3
- D4 pad 4: (no net) -> colb_3
- D40 pad 1: (no net) -> row_2
- D40 pad 2: (no net) -> colr_7
- D40 pad 3: (no net) -> colg_7
- D40 pad 4: (no net) -> colb_7
- D41 pad 1: (no net) -> row_2
- D41 pad 2: (no net) -> colr_8
- D41 pad 3: (no net) -> colg_8
- D41 pad 4: (no net) -> colb_8
- D42 pad 1: (no net) -> row_2
- D42 pad 2: (no net) -> colr_9
- D42 pad 3: (no net) -> colg_9
- D42 pad 4: (no net) -> colb_9
- D43 pad 1: (no net) -> row_2
- D43 pad 2: (no net) -> colr_10
- D43 pad 3: (no net) -> colg_10
- D43 pad 4: (no net) -> colb_10
- D44 pad 1: (no net) -> row_2
- D44 pad 2: (no net) -> colr_11
- D44 pad 3: (no net) -> colg_11
- D44 pad 4: (no net) -> colb_11
- D45 pad 1: (no net) -> row_2
- D45 pad 2: (no net) -> colr_12
- D45 pad 3: (no net) -> colg_12
- D45 pad 4: (no net) -> colb_12
- D49 pad 1: (no net) -> row_3
- D49 pad 2: (no net) -> colr_0
- D49 pad 3: (no net) -> colg_0
- D49 pad 4: (no net) -> colb_0
- D5 pad 1: (no net) -> row_0
- D5 pad 2: (no net) -> colr_4
- D5 pad 3: (no net) -> colg_4
- D5 pad 4: (no net) -> colb_4
- D50 pad 1: (no net) -> row_3
- D50 pad 2: (no net) -> colr_1
- D50 pad 3: (no net) -> colg_1
- D50 pad 4: (no net) -> colb_1
- D51 pad 1: (no net) -> row_3
- D51 pad 2: (no net) -> colr_2
- D51 pad 3: (no net) -> colg_2
- D51 pad 4: (no net) -> colb_2
- D52 pad 1: (no net) -> row_3
- D52 pad 2: (no net) -> colr_3
- D52 pad 3: (no net) -> colg_3
- D52 pad 4: (no net) -> colb_3
- D53 pad 1: (no net) -> row_3
- D53 pad 2: (no net) -> colr_4
- D53 pad 3: (no net) -> colg_4
- D53 pad 4: (no net) -> colb_4
- D54 pad 1: (no net) -> row_3
- D54 pad 2: (no net) -> colr_5
- D54 pad 3: (no net) -> colg_5
- D54 pad 4: (no net) -> colb_5
- D55 pad 1: (no net) -> row_3
- D55 pad 2: (no net) -> colr_6
- D55 pad 3: (no net) -> colg_6
- D55 pad 4: (no net) -> colb_6
- D56 pad 1: (no net) -> row_3
- D56 pad 2: (no net) -> colr_7
- D56 pad 3: (no net) -> colg_7
- D56 pad 4: (no net) -> colb_7
- D57 pad 1: (no net) -> row_3
- D57 pad 2: (no net) -> colr_8
- D57 pad 3: (no net) -> colg_8
- D57 pad 4: (no net) -> colb_8
- D58 pad 1: (no net) -> row_3
- D58 pad 2: (no net) -> colr_9
- D58 pad 3: (no net) -> colg_9
- D58 pad 4: (no net) -> colb_9
- D59 pad 1: (no net) -> row_3
- D59 pad 2: (no net) -> colr_10
- D59 pad 3: (no net) -> colg_10
- D59 pad 4: (no net) -> colb_10
- D6 pad 1: (no net) -> row_0
- D6 pad 2: (no net) -> colr_5
- D6 pad 3: (no net) -> colg_5
- D6 pad 4: (no net) -> colb_5
- D60 pad 1: (no net) -> row_3
- D60 pad 2: (no net) -> colr_11
- D60 pad 3: (no net) -> colg_11
- D60 pad 4: (no net) -> colb_11
- D65 pad 1: (no net) -> row_4
- D65 pad 2: (no net) -> colr_0
- D65 pad 3: (no net) -> colg_0
- D65 pad 4: (no net) -> colb_0
- D66 pad 1: (no net) -> row_4
- D66 pad 2: (no net) -> colr_1
- D66 pad 3: (no net) -> colg_1
- D66 pad 4: (no net) -> colb_1
- D67 pad 1: (no net) -> row_4
- D67 pad 2: (no net) -> colr_2
- D67 pad 3: (no net) -> colg_2
- D67 pad 4: (no net) -> colb_2
- D68 pad 1: (no net) -> row_4
- D68 pad 2: (no net) -> colr_3
- D68 pad 3: (no net) -> colg_3
- D68 pad 4: (no net) -> colb_3
- D69 pad 1: (no net) -> row_4
- D69 pad 2: (no net) -> colr_4
- D69 pad 3: (no net) -> colg_4
- D69 pad 4: (no net) -> colb_4
- D7 pad 1: (no net) -> row_0
- D7 pad 2: (no net) -> colr_6
- D7 pad 3: (no net) -> colg_6
- D7 pad 4: (no net) -> colb_6
- D70 pad 1: (no net) -> row_4
- D70 pad 2: (no net) -> colr_5
- D70 pad 3: (no net) -> colg_5
- D70 pad 4: (no net) -> colb_5
- D71 pad 1: (no net) -> row_4
- D71 pad 2: (no net) -> colr_6
- D71 pad 3: (no net) -> colg_6
- D71 pad 4: (no net) -> colb_6
- D72 pad 1: (no net) -> row_4
- D72 pad 2: (no net) -> colr_7
- D72 pad 3: (no net) -> colg_7
- D72 pad 4: (no net) -> colb_7
- D73 pad 1: (no net) -> row_4
- D73 pad 2: (no net) -> colr_8
- D73 pad 3: (no net) -> colg_8
- D73 pad 4: (no net) -> colb_8
- D74 pad 1: (no net) -> row_4
- D74 pad 2: (no net) -> colr_9
- D74 pad 3: (no net) -> colg_9
- D74 pad 4: (no net) -> colb_9
- D75 pad 1: (no net) -> row_4
- D75 pad 2: (no net) -> colr_10
- D75 pad 3: (no net) -> colg_10
- D75 pad 4: (no net) -> colb_10
- D8 pad 1: (no net) -> row_0
- D8 pad 2: (no net) -> colr_7
- D8 pad 3: (no net) -> colg_7
- D8 pad 4: (no net) -> colb_7
- D81 pad 1: (no net) -> row_5
- D81 pad 2: (no net) -> colr_0
- D81 pad 3: (no net) -> colg_0
- D81 pad 4: (no net) -> colb_0
- D82 pad 1: (no net) -> row_5
- D82 pad 2: (no net) -> colr_1
- D82 pad 3: (no net) -> colg_1
- D82 pad 4: (no net) -> colb_1
- D83 pad 1: (no net) -> row_5
- D83 pad 2: (no net) -> colr_2
- D83 pad 3: (no net) -> colg_2
- D83 pad 4: (no net) -> colb_2
- D84 pad 1: (no net) -> row_5
- D84 pad 2: (no net) -> colr_3
- D84 pad 3: (no net) -> colg_3
- D84 pad 4: (no net) -> colb_3
- D85 pad 1: (no net) -> row_5
- D85 pad 2: (no net) -> colr_4
- D85 pad 3: (no net) -> colg_4
- D85 pad 4: (no net) -> colb_4
- D86 pad 1: (no net) -> row_5
- D86 pad 2: (no net) -> colr_5
- D86 pad 3: (no net) -> colg_5
- D86 pad 4: (no net) -> colb_5
- D87 pad 1: (no net) -> row_5
- D87 pad 2: (no net) -> colr_6
- D87 pad 3: (no net) -> colg_6
- D87 pad 4: (no net) -> colb_6
- D88 pad 1: (no net) -> row_5
- D88 pad 2: (no net) -> colr_7
- D88 pad 3: (no net) -> colg_7
- D88 pad 4: (no net) -> colb_7
- D89 pad 1: (no net) -> row_5
- D89 pad 2: (no net) -> colr_8
- D89 pad 3: (no net) -> colg_8
- D89 pad 4: (no net) -> colb_8
- D9 pad 1: (no net) -> row_0
- D9 pad 2: (no net) -> colr_8
- D9 pad 3: (no net) -> colg_8
- D9 pad 4: (no net) -> colb_8
- D90 pad 1: (no net) -> row_5
- D90 pad 2: (no net) -> colr_9
- D90 pad 3: (no net) -> colg_9
- D90 pad 4: (no net) -> colb_9
- D97 pad 1: (no net) -> row_6
- D97 pad 2: (no net) -> colr_0
- D97 pad 3: (no net) -> colg_0
- D97 pad 4: (no net) -> colb_0
- D98 pad 1: (no net) -> row_6
- D98 pad 2: (no net) -> colr_1
- D98 pad 3: (no net) -> colg_1
- D98 pad 4: (no net) -> colb_1
- D99 pad 1: (no net) -> row_6
- D99 pad 2: (no net) -> colr_2
- D99 pad 3: (no net) -> colg_2
- D99 pad 4: (no net) -> colb_2
- J1 pad 1: (no net) -> vcc
- J1 pad 2: (no net) -> dat
- J1 pad 3: (no net) -> blank
- J1 pad 4: (no net) -> latch
- J1 pad 5: (no net) -> sclk
- J1 pad 6: (no net) -> gnd
- J1 pad SH: (no net) -> gnd
- J2 pad 1: (no net) -> vcc
- J2 pad 2: (no net) -> dat_out
- J2 pad 3: (no net) -> blank
- J2 pad 4: (no net) -> latch
- J2 pad 5: (no net) -> sclk
- J2 pad 6: (no net) -> gnd
- J2 pad SH: (no net) -> gnd
- Q1 pad 1: (no net) -> vcc
- Q1 pad 2: (no net) -> srow_0
- Q1 pad 3: (no net) -> row_0
- Q10 pad 1: (no net) -> vcc
- Q10 pad 2: (no net) -> srow_9
- Q10 pad 3: (no net) -> row_9
- Q11 pad 1: (no net) -> vcc
- Q11 pad 2: (no net) -> srow_10
- Q11 pad 3: (no net) -> row_10
- Q12 pad 1: (no net) -> vcc
- Q12 pad 2: (no net) -> srow_11
- Q12 pad 3: (no net) -> row_11
- Q13 pad 1: (no net) -> vcc
- Q13 pad 2: (no net) -> srow_12
- Q13 pad 3: (no net) -> row_12
- Q14 pad 1: (no net) -> vcc
- Q14 pad 2: (no net) -> srow_13
- Q14 pad 3: (no net) -> row_13
- Q15 pad 1: (no net) -> vcc
- Q15 pad 2: (no net) -> srow_14
- Q15 pad 3: (no net) -> row_14
- Q2 pad 1: (no net) -> vcc
- Q2 pad 2: (no net) -> srow_1
- Q2 pad 3: (no net) -> row_1
- Q3 pad 1: (no net) -> vcc
- Q3 pad 2: (no net) -> srow_2
- Q3 pad 3: (no net) -> row_2
- Q4 pad 1: (no net) -> vcc
- Q4 pad 2: (no net) -> srow_3
- Q4 pad 3: (no net) -> row_3
- Q5 pad 1: (no net) -> vcc
- Q5 pad 2: (no net) -> srow_4
- Q5 pad 3: (no net) -> row_4
- Q6 pad 1: (no net) -> vcc
- Q6 pad 2: (no net) -> srow_5
- Q6 pad 3: (no net) -> row_5
- Q7 pad 1: (no net) -> vcc
- Q7 pad 2: (no net) -> srow_6
- Q7 pad 3: (no net) -> row_6
- Q8 pad 1: (no net) -> vcc
- Q8 pad 2: (no net) -> srow_7
- Q8 pad 3: (no net) -> row_7
- Q9 pad 1: (no net) -> vcc
- Q9 pad 2: (no net) -> srow_8
- Q9 pad 3: (no net) -> row_8
- R1 pad 1: (no net) -> U1_r_ext
- R1 pad 2: (no net) -> gnd
- R2 pad 1: (no net) -> U2_r_ext
- R2 pad 2: (no net) -> gnd
- R3 pad 1: (no net) -> U3_r_ext
- R3 pad 2: (no net) -> gnd
- U1 pad 1: (no net) -> gnd
- U1 pad 10: (no net) -> colr_5
- U1 pad 11: (no net) -> colr_6
- U1 pad 12: (no net) -> colr_7
- U1 pad 13: (no net) -> colr_8
- U1 pad 14: (no net) -> colr_9
- U1 pad 15: (no net) -> colr_10
- U1 pad 16: (no net) -> colr_11
- U1 pad 17: (no net) -> colr_12
- U1 pad 18: (no net) -> colr_13
- U1 pad 19: (no net) -> colr_14
- U1 pad 2: (no net) -> dat
- U1 pad 20: (no net) -> colr_15
- U1 pad 21: (no net) -> blank
- U1 pad 22: (no net) -> sdo_U1>sdi_U2
- U1 pad 23: (no net) -> U1_r_ext
- U1 pad 24: (no net) -> vcc
- U1 pad 3: (no net) -> sclk
- U1 pad 4: (no net) -> latch
- U1 pad 5: (no net) -> colr_0
- U1 pad 6: (no net) -> colr_1
- U1 pad 7: (no net) -> colr_2
- U1 pad 8: (no net) -> colr_3
- U1 pad 9: (no net) -> colr_4
- U2 pad 1: (no net) -> gnd
- U2 pad 10: (no net) -> colg_5
- U2 pad 11: (no net) -> colg_6
- U2 pad 12: (no net) -> colg_7
- U2 pad 13: (no net) -> colg_8
- U2 pad 14: (no net) -> colg_9
- U2 pad 15: (no net) -> colg_10
- U2 pad 16: (no net) -> colg_11
- U2 pad 17: (no net) -> colg_12
- U2 pad 18: (no net) -> colg_13
- U2 pad 19: (no net) -> colg_14
- U2 pad 2: (no net) -> sdo_U1>sdi_U2
- U2 pad 20: (no net) -> colg_15
- U2 pad 21: (no net) -> blank
- U2 pad 22: (no net) -> sdo_U2>sdi_U3
- U2 pad 23: (no net) -> U2_r_ext
- U2 pad 24: (no net) -> vcc
- U2 pad 3: (no net) -> sclk
- U2 pad 4: (no net) -> latch
- U2 pad 5: (no net) -> colg_0
- U2 pad 6: (no net) -> colg_1
- U2 pad 7: (no net) -> colg_2
- U2 pad 8: (no net) -> colg_3
- U2 pad 9: (no net) -> colg_4
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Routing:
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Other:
- board size 105.3 x 45.2 mm -> 36.3 x 32.7 mm
